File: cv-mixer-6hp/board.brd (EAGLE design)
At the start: 30 x 99 mm, 34 parts, among them IC2 TL074P, M1 100k, M2 100k, M3 100k, M4 100k

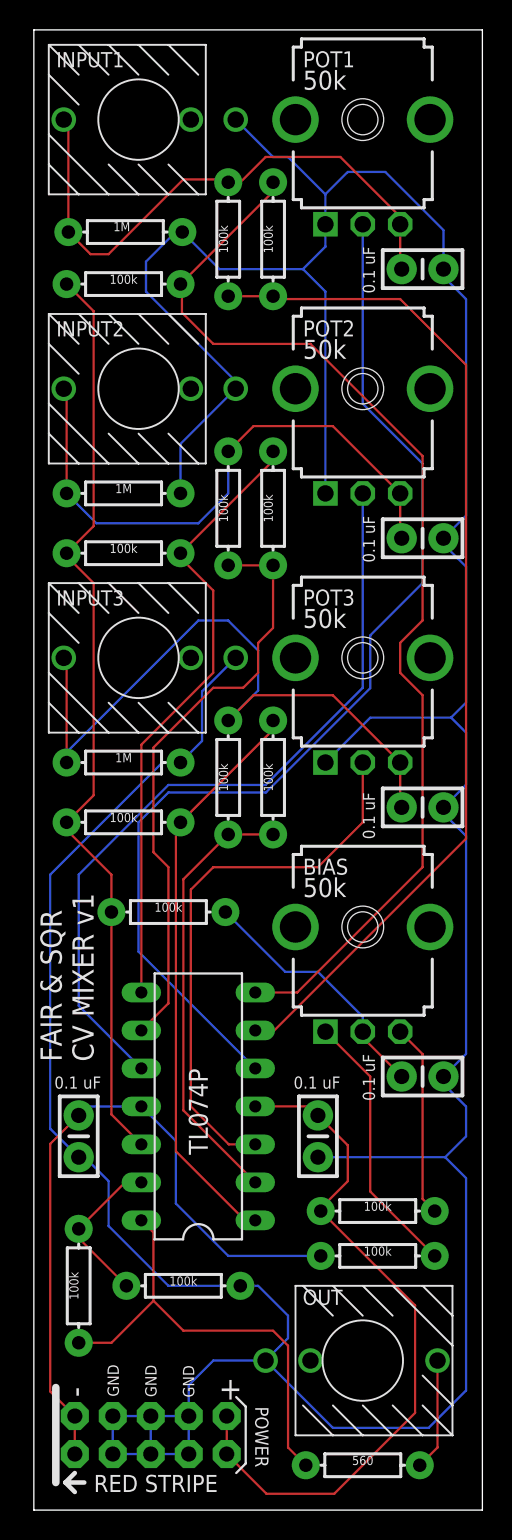
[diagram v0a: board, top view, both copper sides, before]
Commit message: Replace 7hp mixer with 6hp version
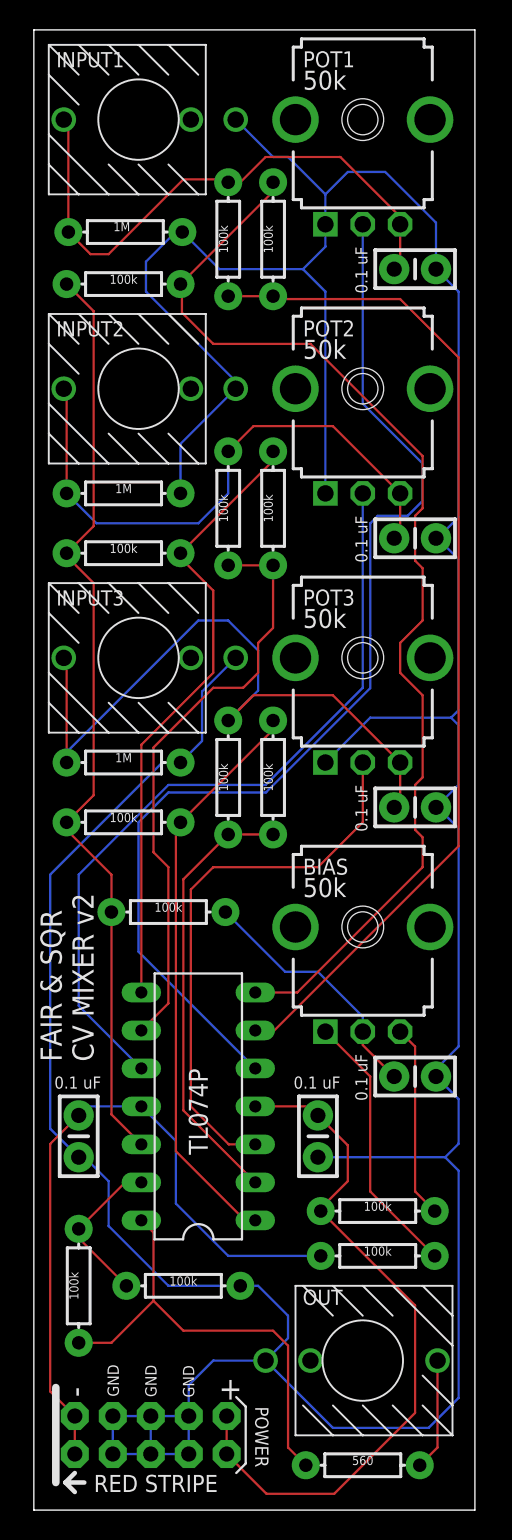
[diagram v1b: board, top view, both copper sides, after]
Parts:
- moved C1 0.50 mm to (25.5, 83.0)
- moved C2 0.50 mm to (25.5, 65.0)
- moved C3 0.50 mm to (25.5, 47.0)
- moved C_BIAS 0.50 mm to (25.5, 29.0)
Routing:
- net N$17: track 73.0 -> 74.2 mm
- net GND: track 279.2 -> 278.1 mm
- net N$14: track 74.8 -> 75.7 mm
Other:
- board size 30 x 99 mm -> 29.5 x 99 mm
- board text added: "FAIR & SQR CV MIXER v2"
- board text removed: "FAIR & SQR CV MIXER v1"
